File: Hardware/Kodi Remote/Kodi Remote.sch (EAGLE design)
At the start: 20 parts

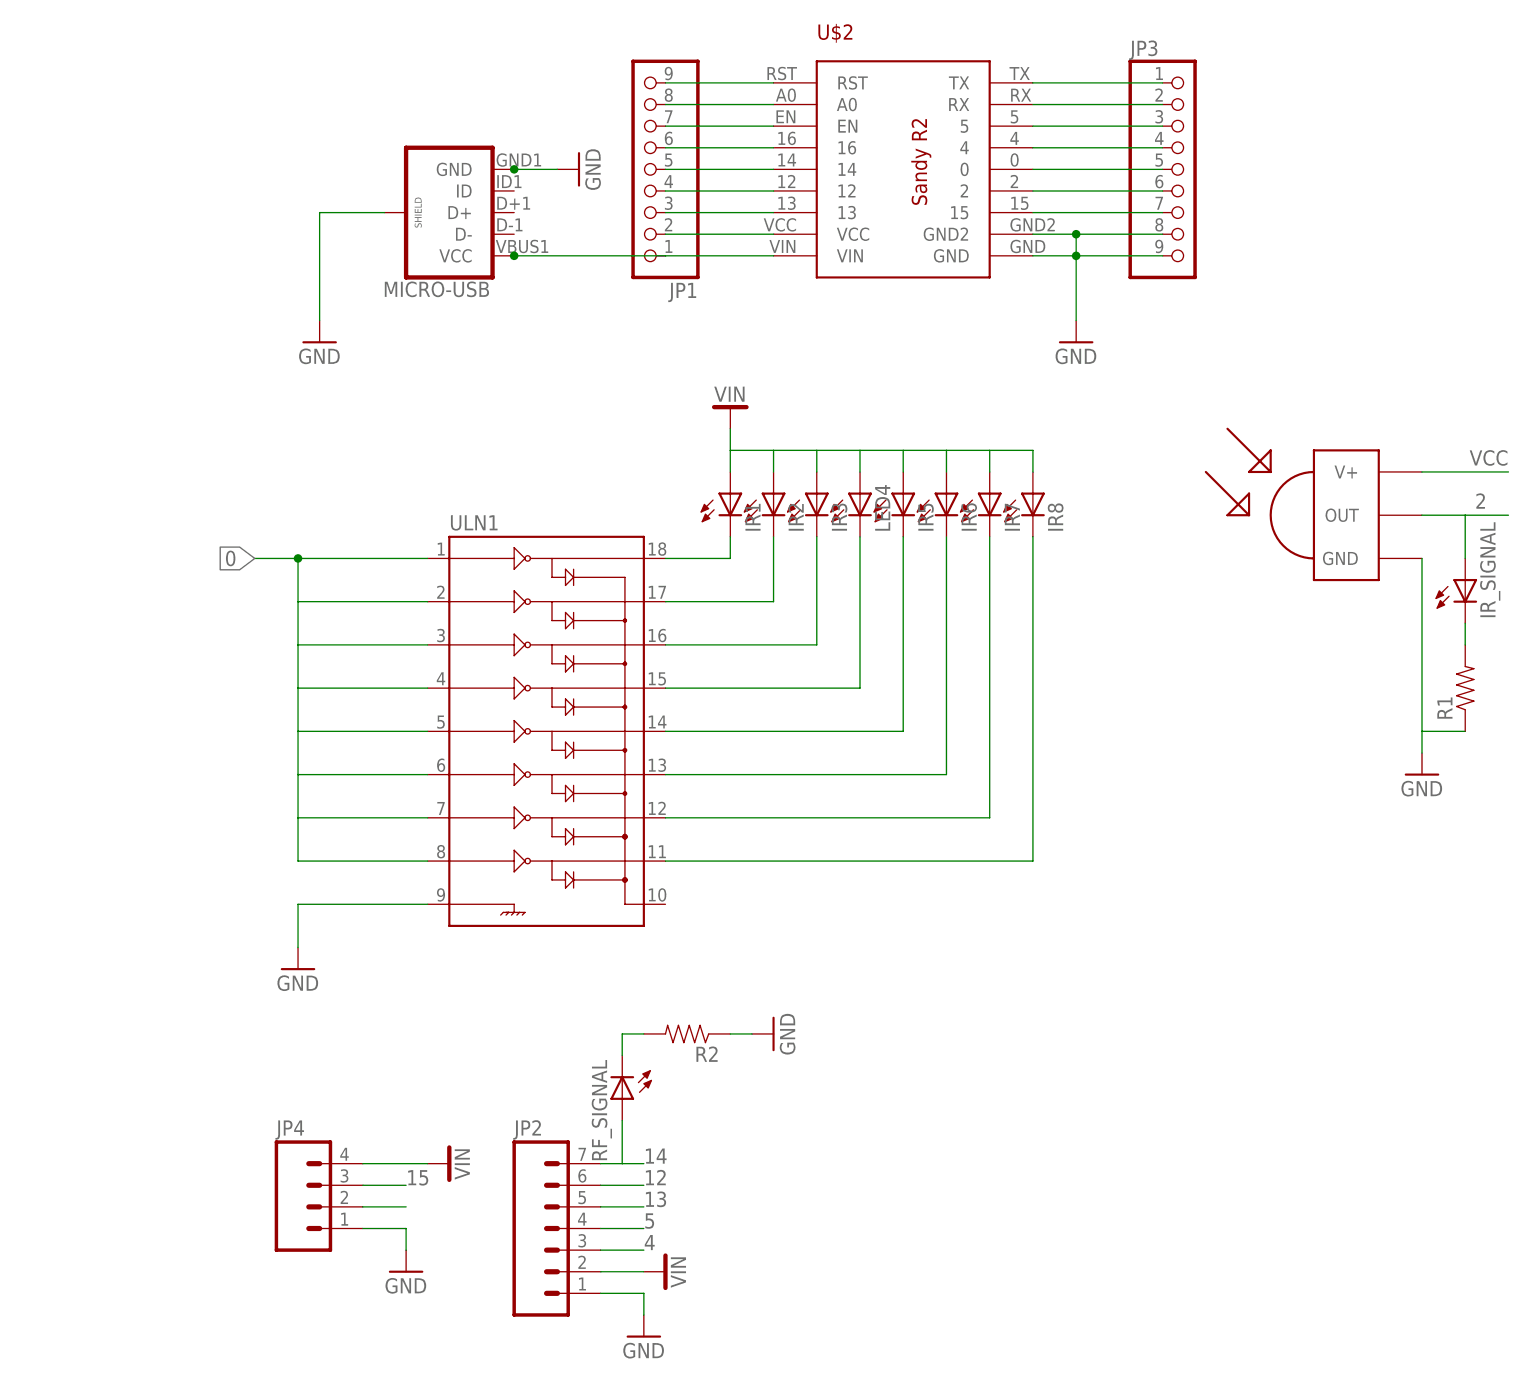
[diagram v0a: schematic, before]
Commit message: Update Kodi Remote
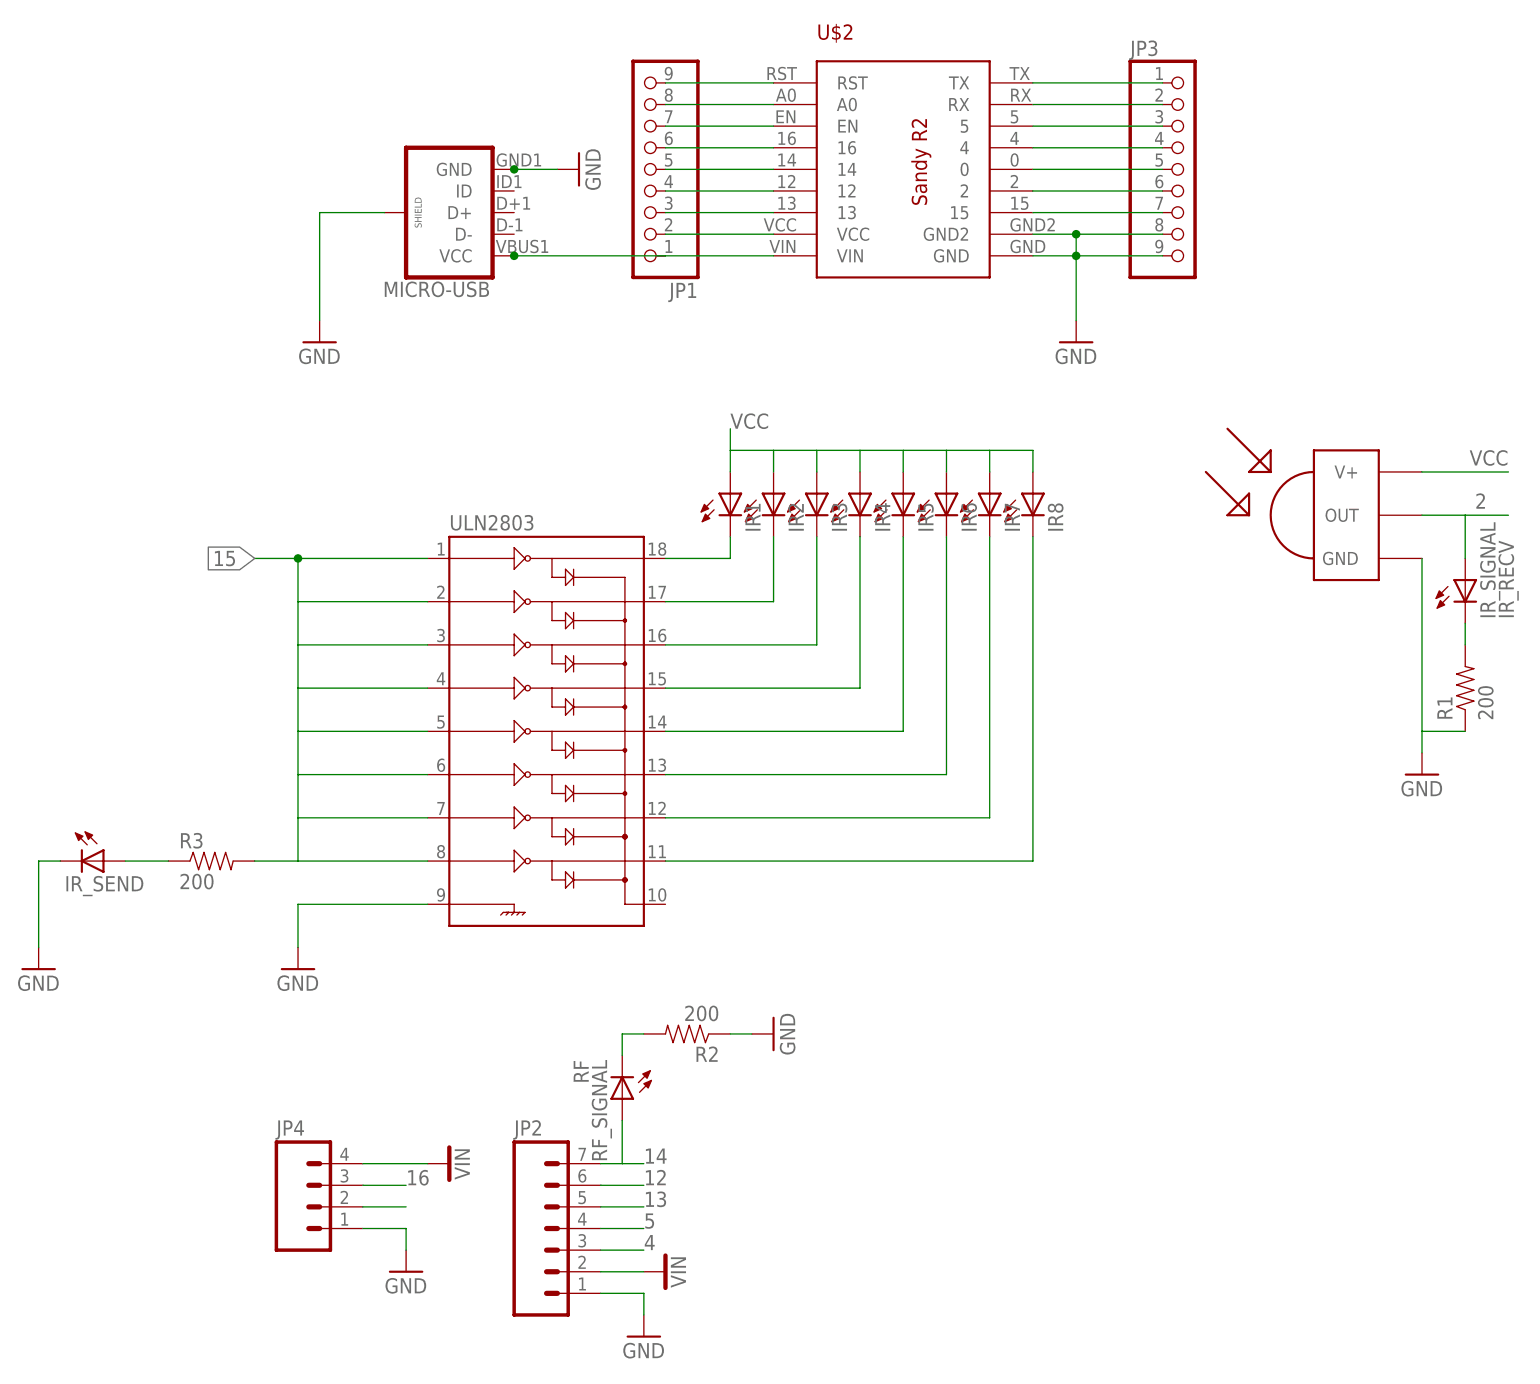
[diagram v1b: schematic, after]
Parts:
- added IR_SEND: (no value), adafruit:LED3MM
- added R3: 200, SparkFun-Resistors:RESISTOR0805-RES
- IR_SIGNAL: value (none) -> IR_RECV; device adafruit:LEDCHIPLED_0805 -> adafruit:LED3MM
- R1, R2: value (none) -> 200
- RF_SIGNAL: value (none) -> RF; device adafruit:LEDCHIPLED_0805 -> adafruit:LED3MM
- renumbered LED4 to IR4, ULN1 to ULN2803
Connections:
- new net N$4: IR_SEND.A, R3.1
- net 0: no longer ULN2803.1, ULN2803.2, ULN2803.3, ULN2803.4, ULN2803.5, ULN2803.6, ULN2803.7, ULN2803.8
- net 15: now also R3.2, ULN2803.1, ULN2803.2, ULN2803.3, ULN2803.4, ULN2803.5, ULN2803.6, ULN2803.7, ULN2803.8; no longer JP4.3
- net 16: now also JP4.3
- net GND: now also IR_SEND.C

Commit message: Update Kodi Remote to use locked version of Sandy Esp
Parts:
- U$2: value MINI-ESP -> MINI-ESPMINI-ESP-LOCK; device My Eagle Lib:MINI-ESP -> My Eagle Lib:MINI-ESPMINI-ESP-LOCK
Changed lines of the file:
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@@
 </classes>
 <parts>
-<part name="U$2" library="My Eagle Lib" deviceset="MINI-ESP" device=""/>
+<part name="U$2" library="My Eagle Lib" deviceset="MINI-ESP" device="MINI-ESP-LOCK" value="MINI-ESPMINI-ESP-LOCK"/>
 <part name="JP1" library="adafruit" deviceset="PINHD-1X9" device=""/>
 <part name="JP3" library="adafruit" deviceset="PINHD-1X9" device=""/>

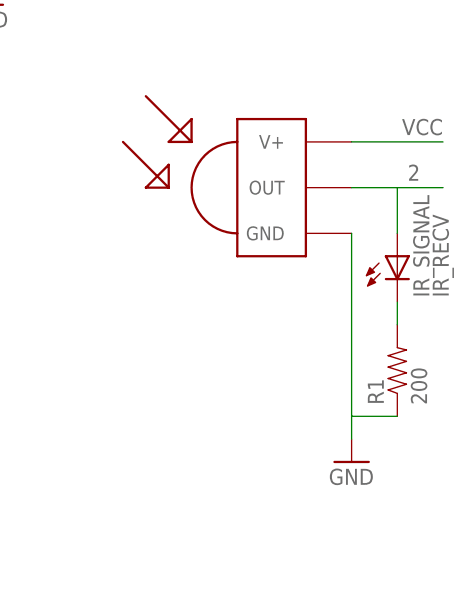
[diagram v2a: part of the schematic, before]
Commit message: Update Kodi after first prototype
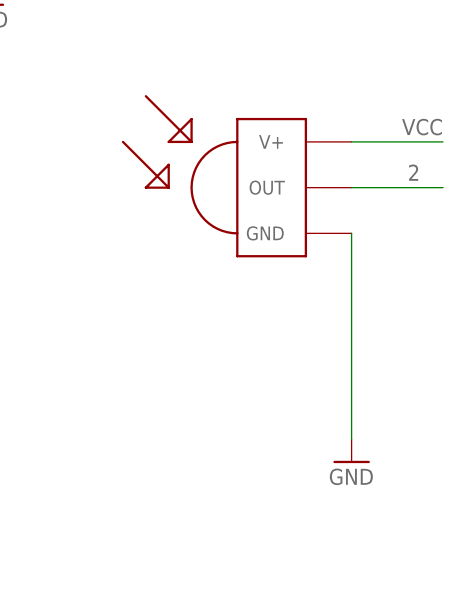
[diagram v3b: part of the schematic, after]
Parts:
- removed IR_SIGNAL: IR_RECV, adafruit:LED3MM
- removed R1: 200, SparkFun-Resistors:RESISTOR0805-RES
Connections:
- removed net N$3: IR_SIGNAL.C, R1.2
- net 2: no longer IR_SIGNAL.A
- net GND: no longer R1.1
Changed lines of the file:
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@@
 <part name="GND6" library="SparkFun" deviceset="GND" device=""/>
 <part name="RF_SIGNAL" library="adafruit" deviceset="LED" device="3MM" value="RF"/>
-<part name="IR_SIGNAL" library="adafruit" deviceset="LED" device="3MM" value="IR_RECV"/>
-<part name="R1" library="SparkFun-Resistors" deviceset="RESISTOR" device="0805-RES" value="200"/>
 <part name="R2" library="SparkFun-Resistors" deviceset="RESISTOR" device="0805-RES" value="200"/>
 <part name="GND7" library="SparkFun" deviceset="GND" device=""/>
@@
 <instance part="GND6" gate="1" x="175.26" y="-73.66"/>
 <instance part="RF_SIGNAL" gate="G$1" x="172.72" y="-45.72" rot="R180"/>
-<instance part="IR_SIGNAL" gate="G$1" x="271.78" y="15.24"/>
-<instance part="R1" gate="G$1" x="271.78" y="2.54" rot="R90"/>
 <instance part="R2" gate="G$1" x="180.34" y="-38.1" rot="R180"/>
 <instance part="GND7" gate="1" x="190.5" y="-38.1" rot="R90"/>
@@
 <segment>
 <pinref part="TSOP1838" gate="G$1" pin="GND"/>
-<wire x1="266.7" y1="17.78" x2="266.7" y2="-2.54" width="0.1524" layer="91"/>
+<wire x1="266.7" y1="17.78" x2="266.7" y2="-5.08" width="0.1524" layer="91"/>
 <pinref part="GND1" gate="1" pin="GND"/>
-<pinref part="R1" gate="G$1" pin="1"/>
-<wire x1="266.7" y1="-2.54" x2="266.7" y2="-5.08" width="0.1524" layer="91"/>
-<wire x1="271.78" y1="-2.54" x2="266.7" y2="-2.54" width="0.1524" layer="91"/>
 </segment>
 <segment>
@@
 <segment>
 <pinref part="TSOP1838" gate="G$1" pin="OUT"/>
-<wire x1="266.7" y1="22.86" x2="271.78" y2="22.86" width="0.1524" layer="91"/>
 <label x="274.32" y="25.4" size="1.778" layer="95" rot="R180"/>
-<pinref part="IR_SIGNAL" gate="G$1" pin="A"/>
-<wire x1="271.78" y1="22.86" x2="276.86" y2="22.86" width="0.1524" layer="91"/>
-<wire x1="271.78" y1="22.86" x2="271.78" y2="17.78" width="0.1524" layer="91"/>
+<wire x1="266.7" y1="22.86" x2="276.86" y2="22.86" width="0.1524" layer="91"/>
 </segment>
 </net>
@@
 </segment>
 </net>
-<net name="N$3" class="0">
-<segment>
-<pinref part="IR_SIGNAL" gate="G$1" pin="C"/>
-<wire x1="271.78" y1="10.16" x2="271.78" y2="7.62" width="0.1524" layer="91"/>
-<pinref part="R1" gate="G$1" pin="2"/>
-</segment>
-</net>
